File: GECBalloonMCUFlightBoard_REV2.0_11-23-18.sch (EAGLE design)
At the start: 51 parts, among them IC1 PIC32MX360F512L, U1 ADS1118, U2 ADS1118, X2 MALE_VGA, Y1 SG-636PCW_50.0000MC3__ROHS

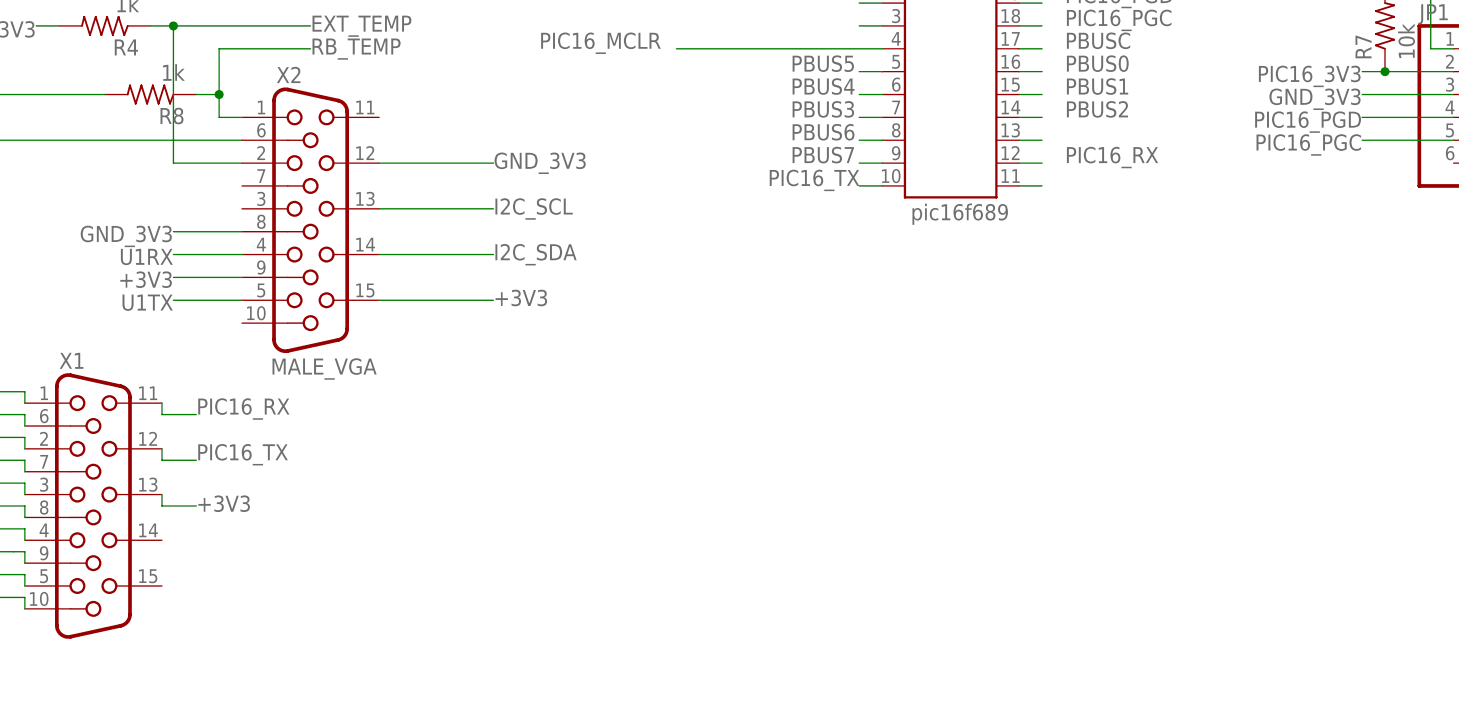
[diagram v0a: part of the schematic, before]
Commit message: Added PIC16_XBEE_SLEEP pin to the VGA connector X1 on PIN14
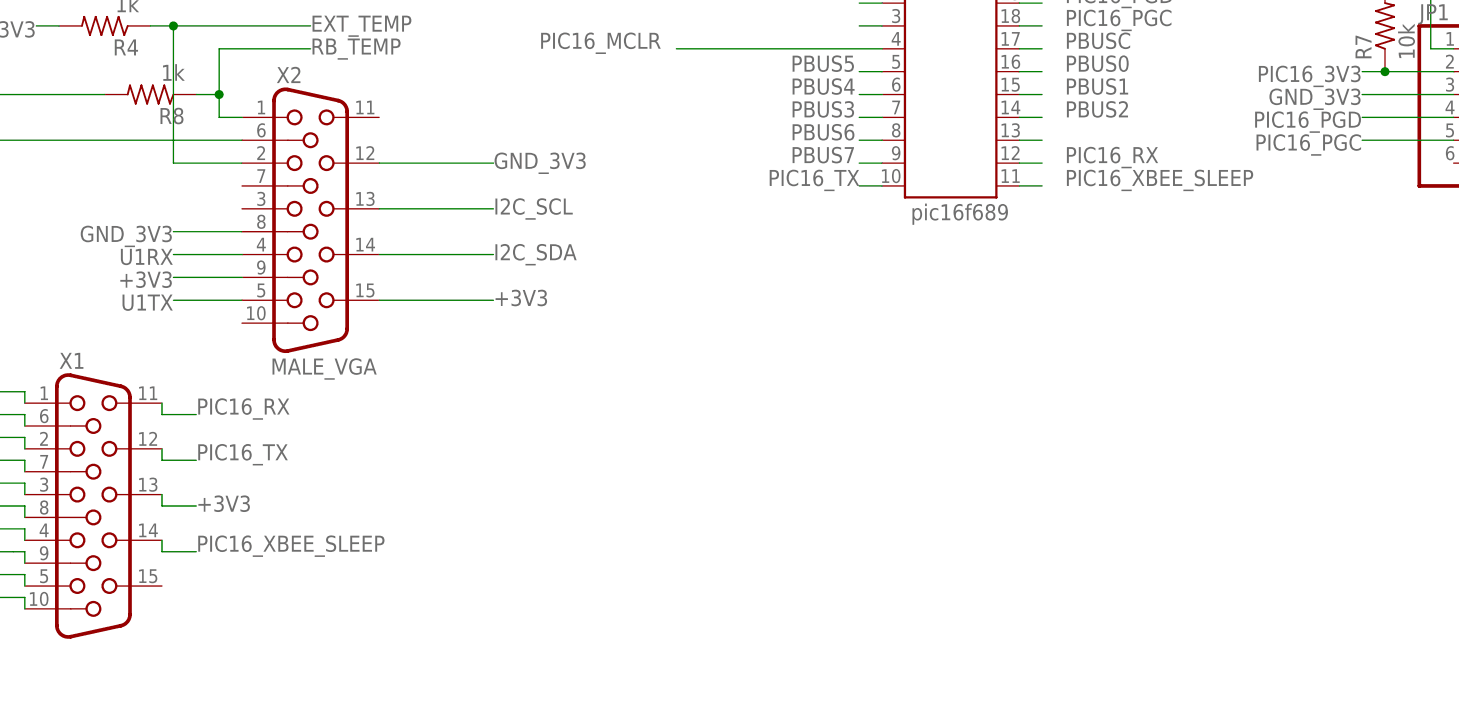
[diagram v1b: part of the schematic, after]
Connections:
- removed net N$20: PIC16.11
- new net PIC16_XBEE_SLEEP: PIC16.11, X1.14
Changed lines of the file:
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@@
-</segment>
-</net>
-<net name="N$20" class="0">
-<segment>
-<pinref part="PIC16" gate="G$1" pin="11"/>
-<wire x1="241.3" y1="-5.08" x2="243.84" y2="-5.08" width="0.1524" layer="91"/>
 </segment>
 </net>
@@
 </segment>
 </net>
+<net name="PIC16_XBEE_SLEEP" class="0">
+<segment>
+<pinref part="X1" gate="G$1" pin="14"/>
+<wire x1="146.05" y1="-44.45" x2="146.05" y2="-45.72" width="0.1524" layer="91"/>
+<wire x1="146.05" y1="-45.72" x2="149.86" y2="-45.72" width="0.1524" layer="91"/>
+<label x="149.86" y="-45.72" size="1.778" layer="95"/>
+</segment>
+<segment>
+<pinref part="PIC16" gate="G$1" pin="11"/>
+<wire x1="241.3" y1="-5.08" x2="243.84" y2="-5.08" width="0.1524" layer="91"/>
+<label x="246.38" y="-5.08" size="1.778" layer="95"/>
+</segment>
+</net>

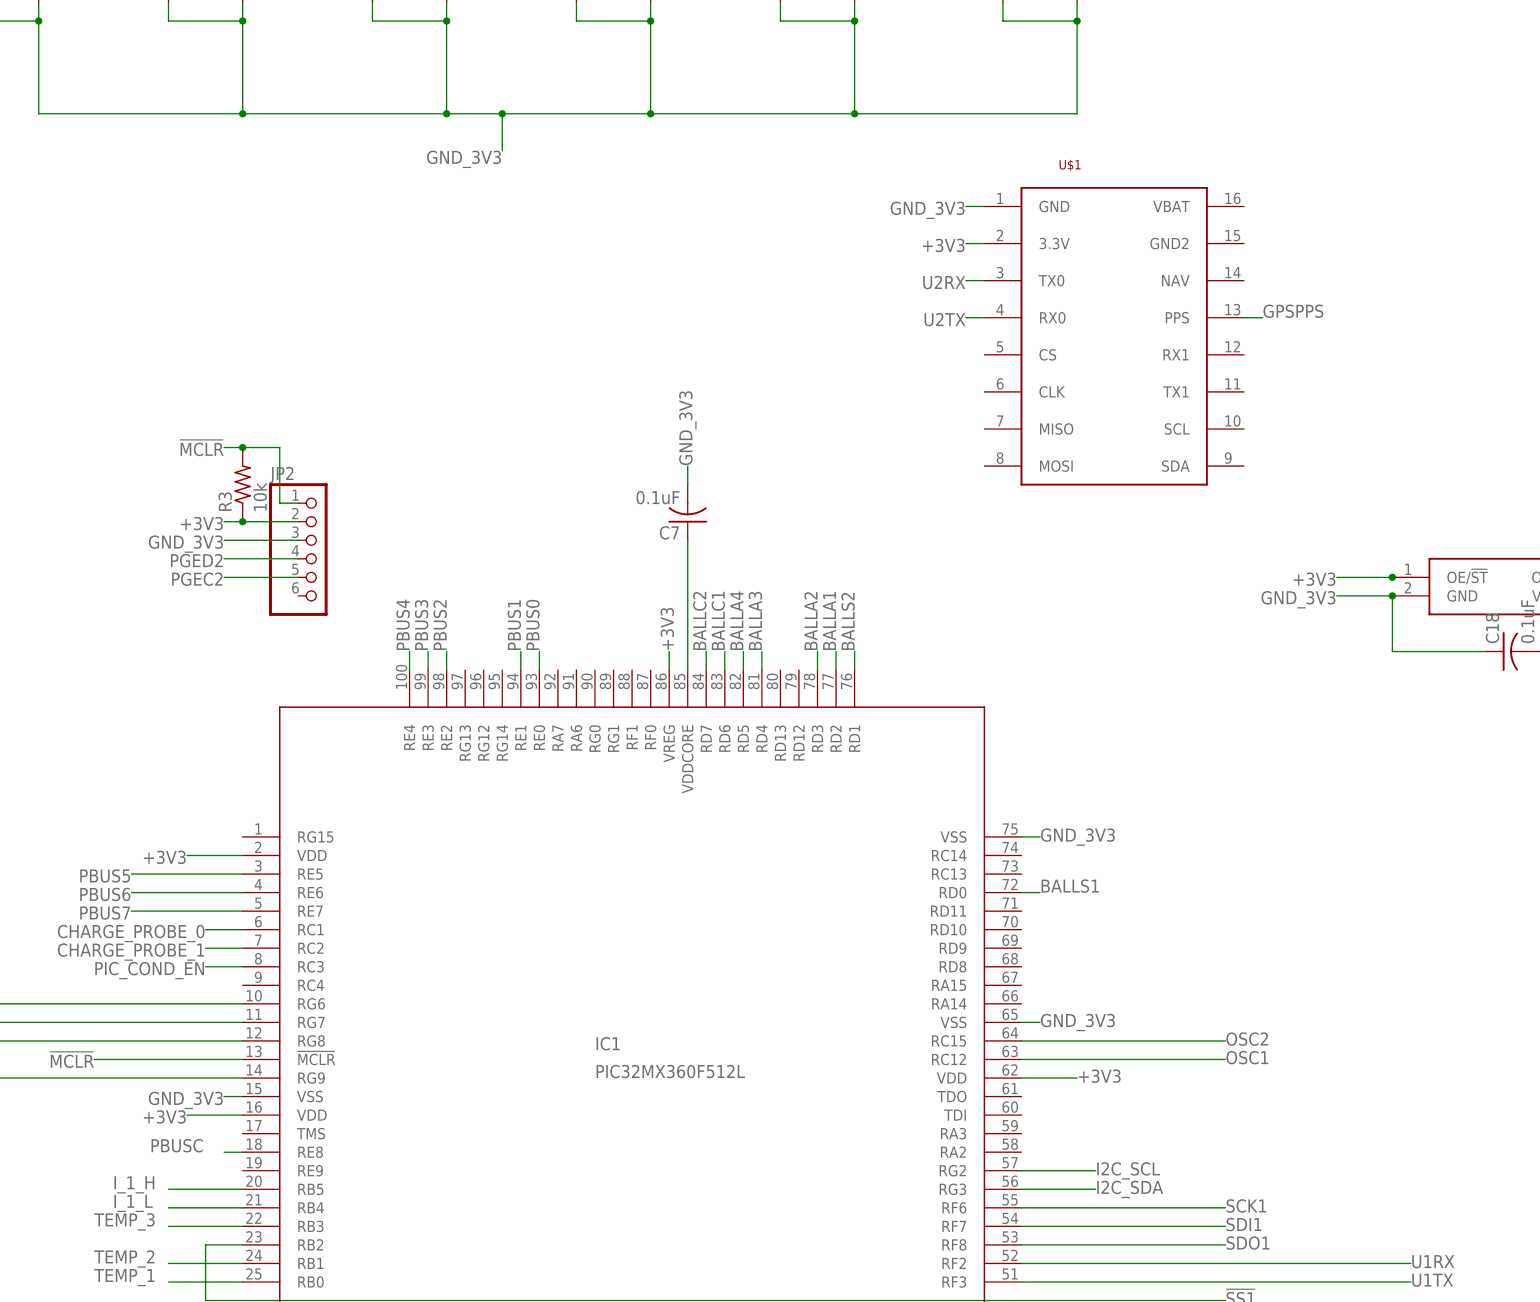
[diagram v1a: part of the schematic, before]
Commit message: Added GPS power mosfet and GPS standby mosfet.
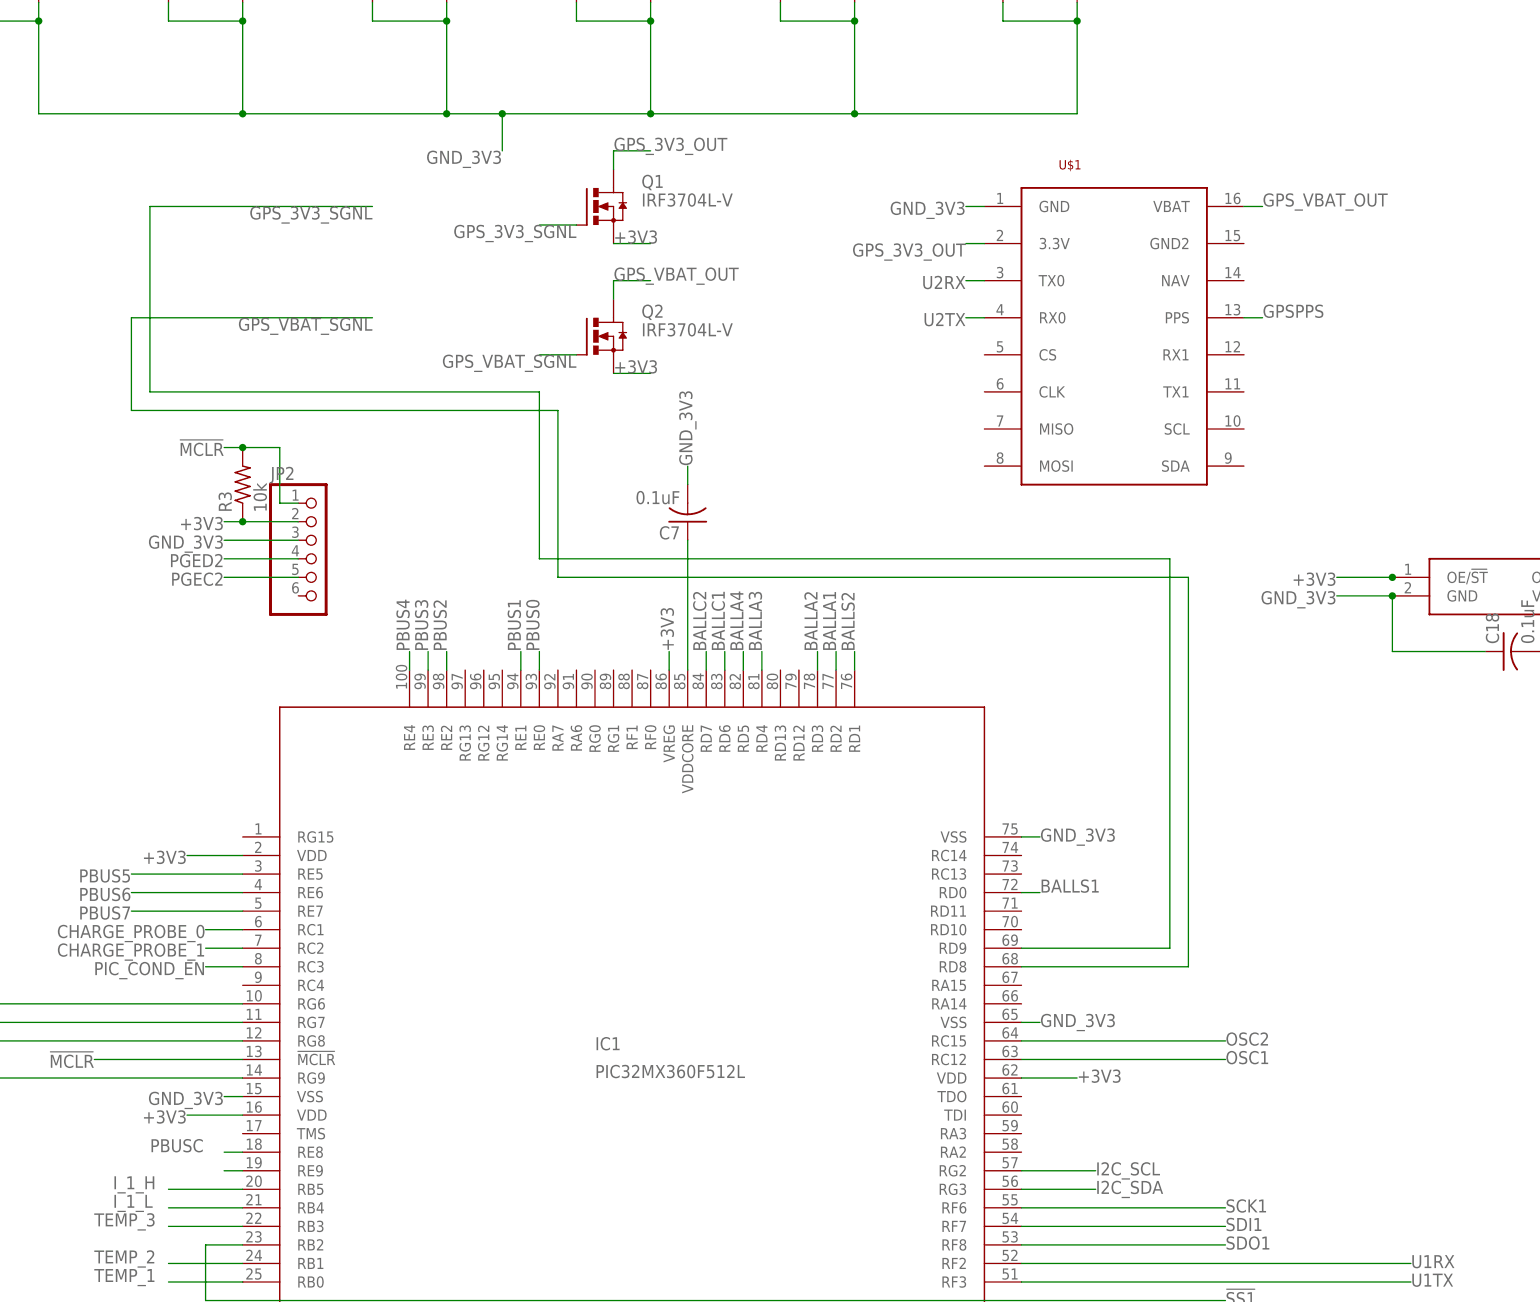
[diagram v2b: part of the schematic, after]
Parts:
- added Q1, Q2: IRF3704L-V, transistor-power:IRF3704L-V
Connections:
- new net GPS_3V3_OUT: Q1.D, U$1.3.3V
- new net GPS_3V3_SGNL: IC1.RD9, Q1.G
- new net GPS_VBAT_OUT: Q2.D, U$1.VBAT
- new net GPS_VBAT_SGNL: IC1.RD8, Q2.G
- new net N$20: IC1.RE9
- net +3V3: now also Q1.S, Q2.S; no longer U$1.3.3V
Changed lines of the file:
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@@
 <part name="Y1" library="SG-636PCW_50.0000MC3__ROHS" deviceset="SG-636PCW_50.0000MC3__ROHS" device=""/>
 <part name="C18" library="resistor" deviceset="C-US" device="C1206" value="0.1uF"/>
+<part name="Q1" library="transistor-power" deviceset="IRF3704" device="L-V"/>
+<part name="Q2" library="transistor-power" deviceset="IRF3704" device="L-V"/>
 </parts>
 <sheets>
@@
 <instance part="Y1" gate="G$1" x="175.26" y="127"/>
 <instance part="C18" gate="G$1" x="190.5" y="116.84" rot="R90"/>
+<instance part="Q1" gate="G$1" x="66.04" y="177.8"/>
+<instance part="Q2" gate="G$1" x="66.04" y="160.02"/>
 </instances>
 <busses>
@@
 </net>
 <net name="+3V3" class="1">
-<segment>
-<pinref part="U$1" gate="G$1" pin="3.3V"/>
-<wire x1="119.38" y1="172.72" x2="116.84" y2="172.72" width="0.1524" layer="91"/>
-<label x="116.84" y="173.355" size="1.778" layer="95" rot="R180"/>
-</segment>
 <segment>
 <pinref part="J2" gate="G$1" pin="B1"/>
@@
 <wire x1="175.26" y1="127" x2="167.64" y2="127" width="0.1524" layer="91"/>
 <label x="167.64" y="127.635" size="1.778" layer="95" rot="R180"/>
+</segment>
+<segment>
+<label x="68.58" y="172.72" size="1.778" layer="95"/>
+<pinref part="Q1" gate="G$1" pin="S"/>
+<wire x1="73.66" y1="172.72" x2="68.58" y2="172.72" width="0.1524" layer="91"/>
+</segment>
+<segment>
+<wire x1="68.58" y1="154.94" x2="73.66" y2="154.94" width="0.1524" layer="91"/>
+<label x="68.58" y="154.94" size="1.778" layer="95"/>
+<pinref part="Q2" gate="G$1" pin="S"/>
 </segment>
 </net>
@@
 </segment>
 </net>
+<net name="GPS_3V3_SGNL" class="0">
+<segment>
+<wire x1="63.5" y1="175.26" x2="58.42" y2="175.26" width="0.1524" layer="91"/>
+<label x="63.5" y="175.26" size="1.778" layer="95" rot="R180"/>
+<pinref part="Q1" gate="G$1" pin="G"/>
+</segment>
+<segment>
+<pinref part="IC1" gate="G$1" pin="RD9"/>
+<wire x1="124.46" y1="76.2" x2="144.78" y2="76.2" width="0.1524" layer="91"/>
+<wire x1="144.78" y1="76.2" x2="144.78" y2="129.54" width="0.1524" layer="91"/>
+<wire x1="144.78" y1="129.54" x2="58.42" y2="129.54" width="0.1524" layer="91"/>
+<wire x1="58.42" y1="129.54" x2="58.42" y2="152.4" width="0.1524" layer="91"/>
+<wire x1="58.42" y1="152.4" x2="5.08" y2="152.4" width="0.1524" layer="91"/>
+<wire x1="5.08" y1="152.4" x2="5.08" y2="177.8" width="0.1524" layer="91"/>
+<wire x1="5.08" y1="177.8" x2="35.56" y2="177.8" width="0.1524" layer="91"/>
+<label x="35.56" y="177.8" size="1.778" layer="95" rot="R180"/>
+</segment>
+</net>
+<net name="GPS_3V3_OUT" class="0">
+<segment>
+<label x="68.58" y="185.42" size="1.778" layer="95"/>
+<pinref part="Q1" gate="G$1" pin="D"/>
+<wire x1="68.58" y1="182.88" x2="68.58" y2="185.42" width="0.1524" layer="91"/>
+<wire x1="68.58" y1="185.42" x2="73.66" y2="185.42" width="0.1524" layer="91"/>
+</segment>
+<segment>
+<pinref part="U$1" gate="G$1" pin="3.3V"/>
+<wire x1="119.38" y1="172.72" x2="116.84" y2="172.72" width="0.1524" layer="91"/>
+<label x="116.84" y="172.72" size="1.778" layer="95" rot="R180"/>
+</segment>
+</net>
+<net name="GPS_VBAT_SGNL" class="0">
+<segment>
+<wire x1="63.5" y1="157.48" x2="58.42" y2="157.48" width="0.1524" layer="91"/>
+<label x="63.5" y="157.48" size="1.778" layer="95" rot="R180"/>
+<pinref part="Q2" gate="G$1" pin="G"/>
+</segment>
+<segment>
+<wire x1="2.54" y1="162.56" x2="35.56" y2="162.56" width="0.1524" layer="91"/>
+<label x="35.56" y="162.56" size="1.778" layer="95" rot="R180"/>
+<wire x1="2.54" y1="162.56" x2="2.54" y2="149.86" width="0.1524" layer="91"/>
+<wire x1="2.54" y1="149.86" x2="60.96" y2="149.86" width="0.1524" layer="91"/>
+<wire x1="60.96" y1="149.86" x2="60.96" y2="127" width="0.1524" layer="91"/>
+<wire x1="60.96" y1="127" x2="147.32" y2="127" width="0.1524" layer="91"/>
+<wire x1="147.32" y1="127" x2="147.32" y2="73.66" width="0.1524" layer="91"/>
+<pinref part="IC1" gate="G$1" pin="RD8"/>
+<wire x1="147.32" y1="73.66" x2="124.46" y2="73.66" width="0.1524" layer="91"/>
+</segment>
+</net>
+<net name="GPS_VBAT_OUT" class="0">
+<segment>
+<wire x1="68.58" y1="165.1" x2="68.58" y2="167.64" width="0.1524" layer="91"/>
+<label x="68.58" y="167.64" size="1.778" layer="95"/>
+<wire x1="68.58" y1="167.64" x2="73.66" y2="167.64" width="0.1524" layer="91"/>
+<pinref part="Q2" gate="G$1" pin="D"/>
+</segment>
+<segment>
+<pinref part="U$1" gate="G$1" pin="VBAT"/>
+<wire x1="154.94" y1="177.8" x2="157.48" y2="177.8" width="0.1524" layer="91"/>
+<label x="157.48" y="177.8" size="1.778" layer="95"/>
+</segment>
+</net>
+<net name="N$20" class="0">
+<segment>
+<pinref part="IC1" gate="G$1" pin="RE9"/>
+<wire x1="17.78" y1="45.72" x2="15.24" y2="45.72" width="0.1524" layer="91"/>
+</segment>
+</net>

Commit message: So far, manage to rip up old traces without totally losing the PIC32's fan out
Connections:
- removed net ADC2_DIN: JP5.5, R12.1, V2/2.Y
- removed net ADC2_SCK: JP6.1, R14.2, V2/1.Y
- removed net PIC_COND_EN: IC1.RC3, V2/4.A
- removed net SCK2: IC1.RG6, V2/1.A
- removed net SDO2: IC1.RG8, V2/2.A
- new net N$67: U1.CS
- new net N$69: JP4.2
- new net N$70: U2.CS
- new net N$79: JP6.2
- new net N/A1: IC1.RC1
- new net N/A2: IC1.RC2
- new net N/A3: IC1.RC3
- new net PIC_CHARGE_PROBE_0: IC1.RG6
- new net PIC_CHARGE_PROBE_1: IC1.RG7
- new net PIC_COND_EN_NEW2: IC1.RG8
- net ADC1_DIN: now also JP5.5, R12.1, V2/2.Y
- net ADC1_DOUT: now also R13.1
- net ADC1_SCK: now also JP6.1, R14.2, V2/1.Y
- net ADC2_DOUT: no longer R13.1
- net CHARGE_PROBE_0: no longer IC1.RC1
- net CHARGE_PROBE_1: no longer IC1.RC2
- net GND_5V: no longer JP4.2, JP6.2, U1.CS, U2.CS
- net SDI2: no longer IC1.RG7

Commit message: Part way done
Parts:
- added R1, R18: 680, resistor:R-US_R1206
- added R15, R19: 510, resistor:R-US_R1206
- R16: value 510 -> 680
- R17: value 680 -> 510
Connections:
- removed net ADC2_DIVIDED: R16.1, R17.2, V2/3.A
- removed net ADC2_DOUT: JP5.4, R16.2
- removed net N$67: U1.CS
- removed net N$69: JP4.2
- removed net N$70: U2.CS
- removed net N$79: JP6.2
- removed net PIC_COND_EN_NEW2: IC1.RG8
- removed net SDI2: V2/3.Y
- new net !SS1_5V: JP4.2, U1.CS, V2/3.Y
- new net !SS2_5V: JP6.2, U2.CS, V2/4.Y
- new net CHRG_PRB_0_5V: R17.1, V2/1.Y
- new net CHRG_PRB_1_5V: R19.1, V2/2.Y
- new net COND_EN_5V: R15.1, V1/4.Y
- new net PIC_COND_EN: IC1.RG8, V1/4.A
- net !SS1: now also V2/3.A
- net !SS2: now also V2/4.A
- net ADC1_DIN: no longer V2/2.Y
- net ADC1_DOUT: now also JP5.4
- net ADC1_SCK: no longer V2/1.Y
- net CHARGE_PROBE_0: now also R16.2, R17.2
- net CHARGE_PROBE_1: now also R18.2, R19.2
- net CONDUCTIVITY_ENABLE: now also R1.2, R15.2; no longer V2/4.Y
- net GND_5V: now also R1.1, R16.1, R18.1; no longer R17.1, V1/4.A, V1/4.Y
- net PIC_CHARGE_PROBE_0: now also V2/1.A
- net PIC_CHARGE_PROBE_1: now also V2/2.A
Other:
- moved on the sheet: R16, R17, V2/1, V2/2, V2/3

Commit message: Routed a lot of signals, fixed a lot of errors and nearly lost my mind. Everything on my checklist is complete now, though.
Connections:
- net N$20 renamed RE9
- net N/A1 renamed RC1
- net N/A2 renamed RC2
- net N/A3 renamed RC3
- new net RC4: IC1.RC4
- new net RG15: IC1.RG15
- new net TMS: IC1.TMS
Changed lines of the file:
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@@
 <pinref part="IC1" gate="G$1" pin="RE8"/>
 <wire x1="17.78" y1="48.26" x2="15.24" y2="48.26" width="0.1524" layer="91"/>
-<label x="5.08" y="48.26" size="1.778" layer="95"/>
+<label x="14.986" y="49.276" size="1.778" layer="95" rot="R180"/>
 </segment>
 </net>
@@
 </segment>
 </net>
-<net name="N$20" class="0">
+<net name="RE9" class="0">
 <segment>
 <pinref part="IC1" gate="G$1" pin="RE9"/>
 <wire x1="17.78" y1="45.72" x2="15.24" y2="45.72" width="0.1524" layer="91"/>
+<label x="15.24" y="46.99" size="1.778" layer="95" rot="R180"/>
 </segment>
 </net>
@@
 </segment>
 </net>
-<net name="N/A1" class="0">
+<net name="RC1" class="0">
 <segment>
 <pinref part="IC1" gate="G$1" pin="RC1"/>
@@
 </segment>
 </net>
-<net name="N/A2" class="0">
+<net name="RC2" class="0">
 <segment>
 <pinref part="IC1" gate="G$1" pin="RC2"/>
@@
 </segment>
 </net>
-<net name="N/A3" class="0">
+<net name="RC3" class="0">
 <segment>
 <pinref part="IC1" gate="G$1" pin="RC3"/>
@@
 </segment>
 </net>
+<net name="RG15" class="0">
+<segment>
+<pinref part="IC1" gate="G$1" pin="RG15"/>
+<wire x1="17.78" y1="91.44" x2="10.16" y2="91.44" width="0.1524" layer="91"/>
+<label x="10.16" y="91.44" size="1.778" layer="95" rot="R180"/>
+</segment>
+</net>
+<net name="RC4" class="0">
+<segment>
+<pinref part="IC1" gate="G$1" pin="RC4"/>
+<wire x1="17.78" y1="71.12" x2="12.7" y2="71.12" width="0.1524" layer="91"/>
+<label x="12.7" y="72.136" size="1.778" layer="95" rot="R180"/>
+</segment>
+</net>
+<net name="TMS" class="0">
+<segment>
+<pinref part="IC1" gate="G$1" pin="TMS"/>
+<wire x1="17.78" y1="50.8" x2="10.16" y2="50.8" width="0.1524" layer="91"/>
+<label x="10.16" y="51.816" size="1.778" layer="95" rot="R180"/>
+</segment>
+</net>
